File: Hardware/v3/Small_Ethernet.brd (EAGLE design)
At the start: 64.5 x 33.4 mm, 57 parts, among them U1 EDISON_CONNECTOR_FULLMOUNTING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, U2 LAN9512-JZX, U3 MAX4995AAUT+, U4 EDISON_CONNECTOR_FULLHEADER, X1 J1011F01P

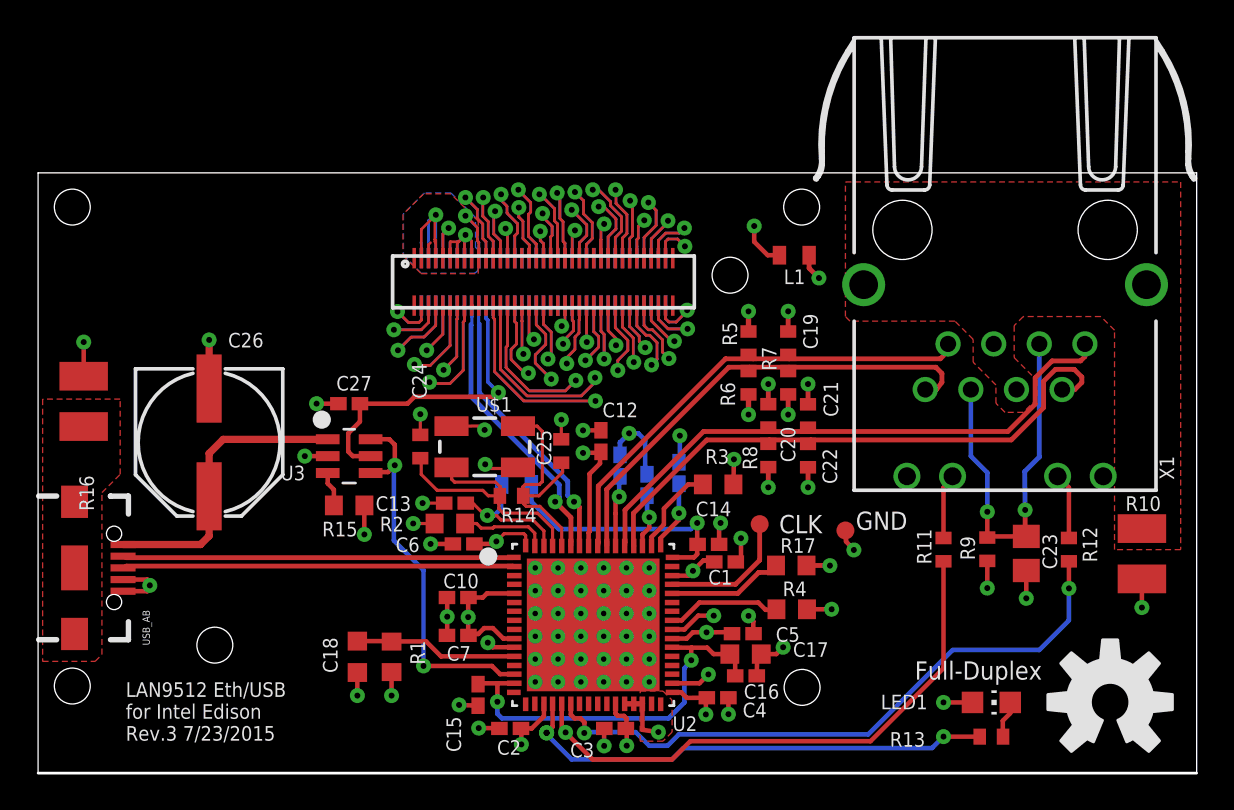
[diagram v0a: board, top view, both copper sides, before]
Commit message: Added ground fills. PoE: power planes around U7, diode for power through microB. Small: changed C26 to 2 caps, removed NP caps, removed test points, replaced crystal
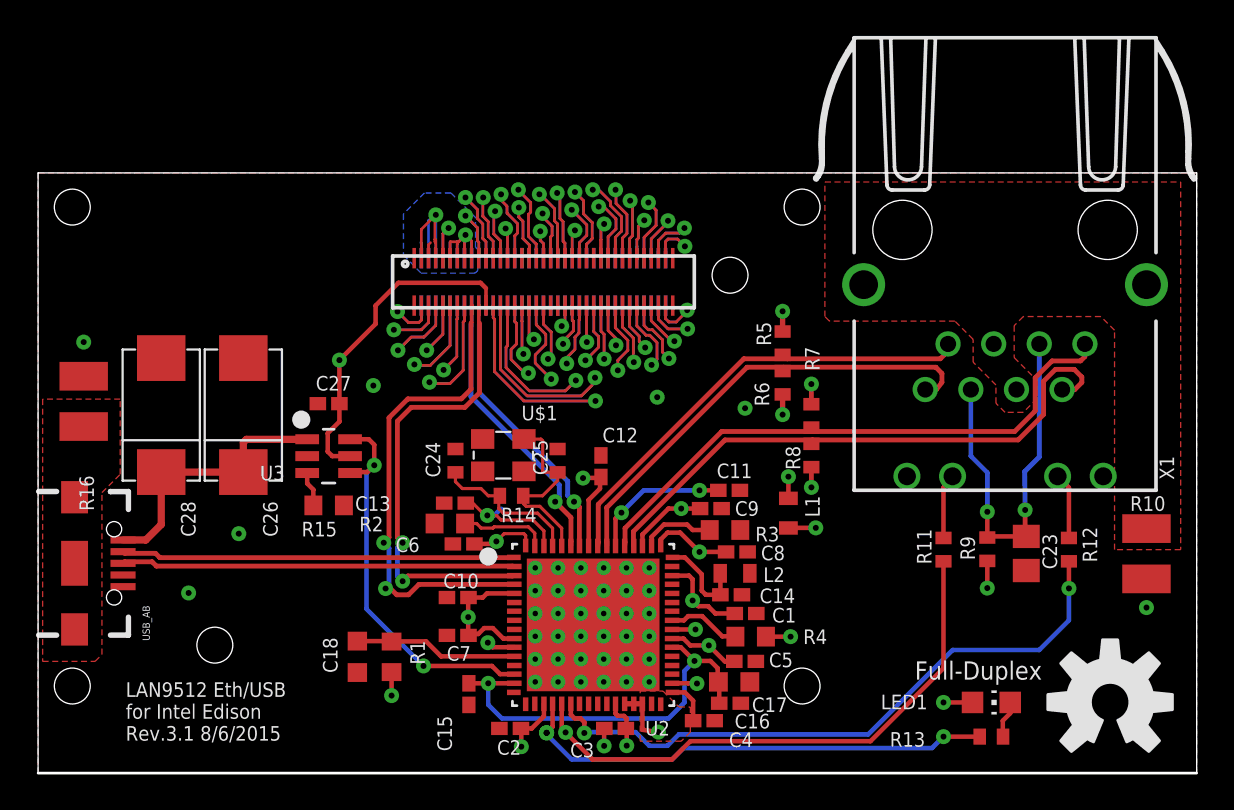
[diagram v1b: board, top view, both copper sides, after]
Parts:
- removed C19, C20, C21, C22: 15pF, rcl:C0402
- removed CLK_PAD: CLK, testpad:TP10R
- removed GNDPAD: GNDPAD, testpad:TP10R
- removed R17: 10K, resistor:R0603
- added C28: (no value), PoEdev:CAP-2917
- C26: value 150uF -> (none); device SparkFun-Capacitors:PANASONIC_E -> PoEdev:CAP-2917
- U$1: value 25MHz -> (none); device SparkFun-FreqCtrl:CRYSTAL-SMD-5X3 -> PoEdev:SMDCRYSTAL_3.2X2.5
- moved L1 14.4 mm to (41.8, 14.5), turned to 90 degrees
- moved L2 13.1 mm to (38.8, 11.1), flipped to the top
- moved C11 6.23 mm to (38.5, 15.7), flipped to the top, turned to 0 degrees
- moved C8 5.45 mm to (38.9, 12.3), flipped to the top, turned to 0 degrees
- moved C9 3.80 mm to (37.5, 14.7), flipped to the top, turned to 0 degrees
- moved C1 3.09 mm to (39.4, 8.89)
- moved C14 3.08 mm to (38.6, 9.93)
- moved R4 2.75 mm to (39.7, 7.60)
- moved R3 2.57 mm to (38.3, 13.5)
- moved C26 2.44 mm to (11.4, 19.9)
- moved R7 2.40 mm to (43.1, 19.9)
- moved R8 2.40 mm to (43.1, 17.7)
- moved C24 2.11 mm to (23.2, 17.4)
- moved R5 1.90 mm to (41.5, 23.9)
- moved R6 1.90 mm to (41.5, 21.7)
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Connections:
- removed net S$3: U4.16
- removed net S$6: U4.20
- new net USB_D_N: U2.3, U4.18
- new net USB_D_P: U2.4, U4.16
- net CLKOUT: no longer CLK_PAD.TP
- net GND: now also C26.NEG, C28.NEG, U$1.P2_GND, U$1.P4_GND; no longer C19.2, C20.2, C21.2, C22.2, C26.-, GNDPAD.TP, U$1.2, U$1.4, USB_AB.ID1
- net N$21: now also U$1.P1_I/O; no longer U$1.1
- net N$22: now also U$1.P3_O/I; no longer U$1.3
- net RX_N: no longer C22.1
- net RX_P: no longer C21.1
- net S$4: no longer R17.1
- net TX_N: no longer C19.1
- net TX_P: no longer C20.1
- net USB_VBUS: now also U4.20
- net VBUS_OUT: now also C26.POS, C28.POS; no longer C26.+
- net VDD3IO: no longer R17.2
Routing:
- net GND: track 78.6 -> 25.1 mm, vias 73 -> 47
- net USB_D_P: track 0.00 -> 27.4 mm, vias 0 -> 2
- net USB_D_N: track 0.00 -> 25.7 mm, vias 0 -> 2
- net N$2: track 14.2 -> 5.26 mm, vias 1 -> 0
- net CLKOUT: track 7.44 -> 0.00 mm
- net S$4: track 6.68 -> 0.00 mm
- net N$21: track 15.0 -> 8.48 mm
- net N$22: track 13.4 -> 10.5 mm
- net N$9: track 6.39 -> 4.10 mm
- net N$1: track 8.11 -> 6.75 mm
- net VBUS_OUT: track 16.5 -> 15.3 mm
- net USB_VBUS: track 17.4 -> 18.4 mm
- net N$8: track 5.10 -> 4.16 mm
- net TX_N: track 26.9 -> 26.1 mm
- net TX_P: track 26.9 -> 26.0 mm
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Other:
- board text added: "LAN9512 Eth/USB for Intel Edison Rev.3.1 8/6/2015"
- board text removed: "CLK"
- board text removed: "GND"
- board text removed: "LAN9512 Eth/USB for Intel Edison Rev.3 7/23/2015"

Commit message: Ready for final review
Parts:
- moved L1 3.78 mm to (43.1, 10.9)
- moved C26 2.85 mm to (12.4, 17.3)
- moved C28 2.85 mm to (7.87, 17.3)
- moved C23 1.82 mm to (55.0, 10.4)
- moved R9 1.80 mm to (52.8, 10.7)
- moved R6 1.78 mm to (41.5, 20.0)
- moved U1 1.78 mm to (40.5, 28.9)
- moved R10 1.78 mm to (61.7, 10.4)
- moved R11 1.78 mm to (50.4, 10.7)
- moved R12 1.78 mm to (57.4, 10.7)
- moved R8 1.78 mm to (43.1, 15.9)
- moved R5 1.78 mm to (41.5, 22.2)
- moved R7 1.78 mm to (43.1, 18.1)
- moved U4 1.78 mm to (28.1, 25.6)
- moved X1 1.78 mm to (53.8, 22.1)
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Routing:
- net N$1: track 6.75 -> 27.5 mm, vias 1 -> 2
- net P24: track 20.0 -> 5.62 mm
- net P26: track 16.3 -> 3.11 mm
- net P22: track 20.0 -> 9.33 mm
- net USB_D_P: track 27.4 -> 24.1 mm
- net USB_D_N: track 25.7 -> 22.4 mm
- net P12: track 7.80 -> 4.94 mm
- net VDD33A: track 52.9 -> 55.5 mm
- net P14: track 11.7 -> 9.17 mm
- net USB_VBUS: track 18.4 -> 16.3 mm
- net N$21: track 8.48 -> 10.4 mm
- net P6: track 7.56 -> 9.38 mm
- net USBUP_P: track 16.0 -> 14.2 mm
- net N$18: track 35.6 -> 33.9 mm
- net USBUP_N: track 15.7 -> 14.0 mm
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- added copper zone on layer 3, net GND
- removed copper zone on layer 3, net USB_REF
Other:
- board size 64.5 x 33.4 mm -> 64.5 x 31.6 mm

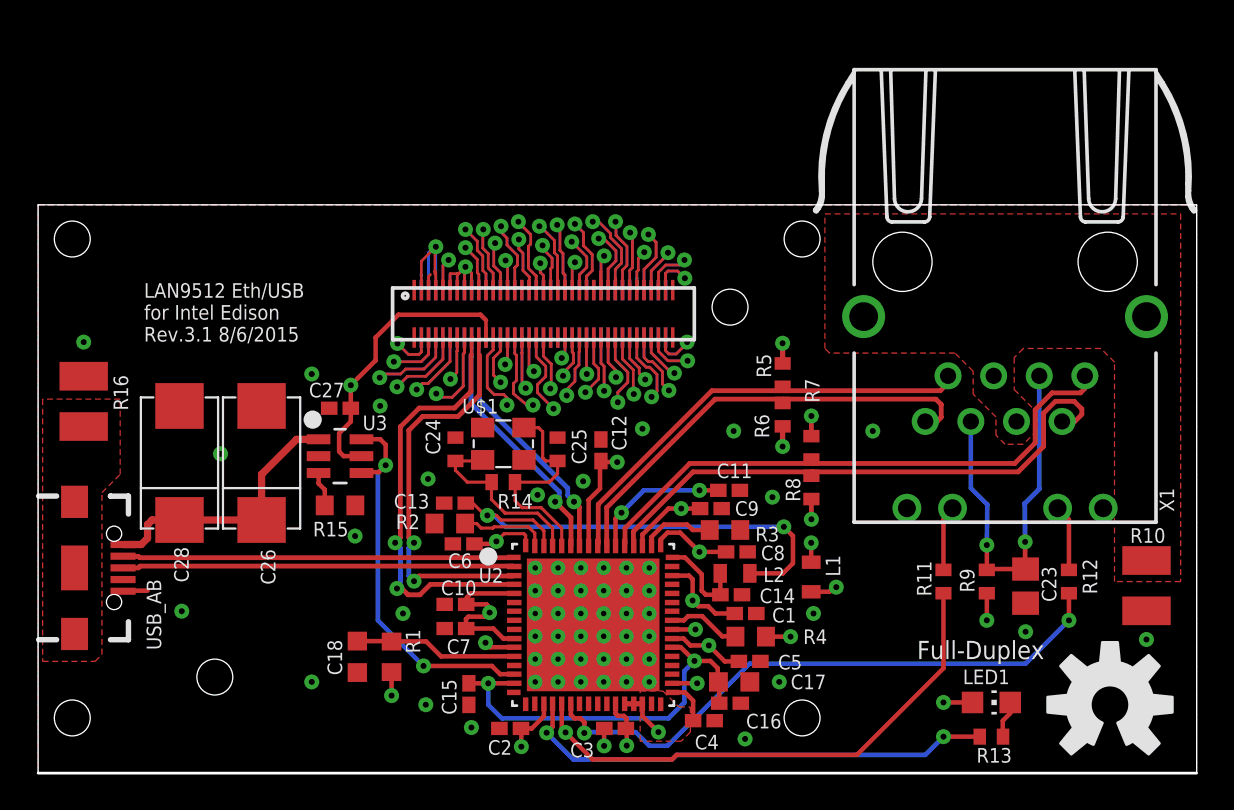
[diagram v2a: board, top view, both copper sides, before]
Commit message: Made downstream USB traces the same length; minor changes to PoE board
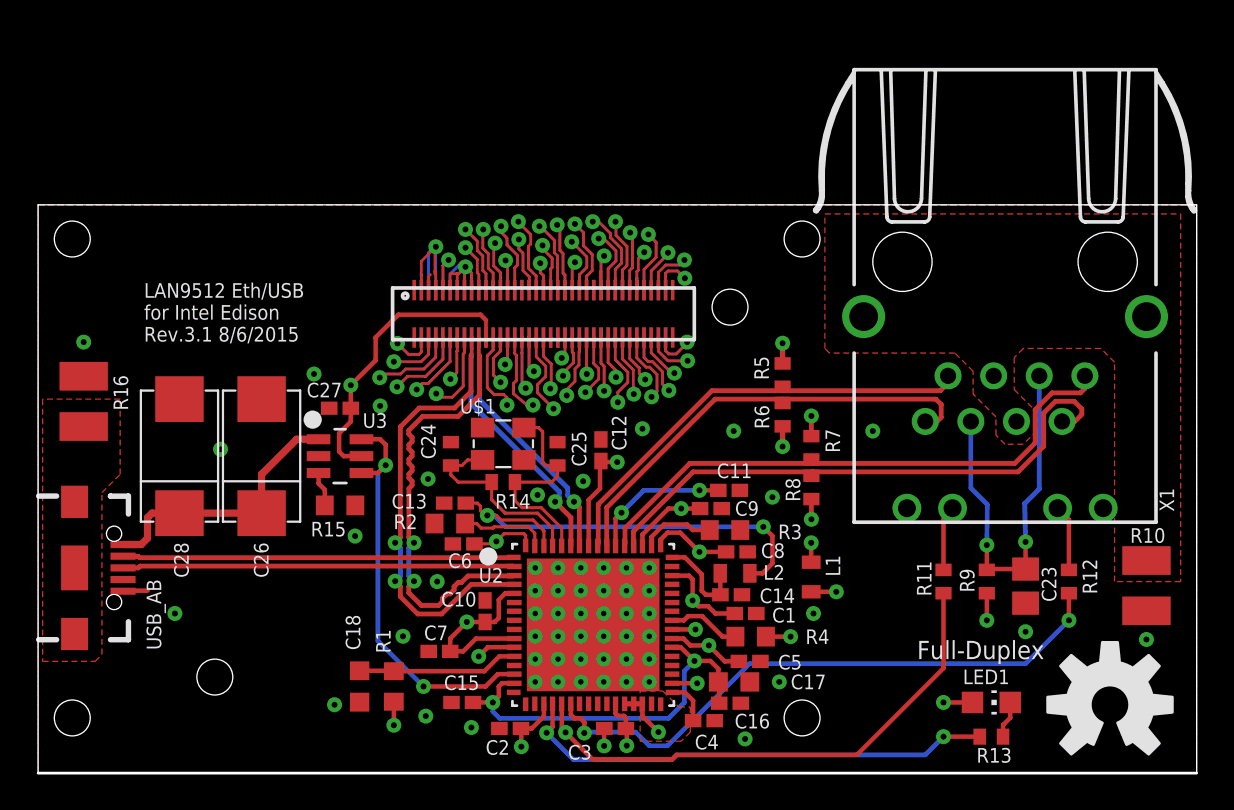
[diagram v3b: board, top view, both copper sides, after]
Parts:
- moved C10 1.69 mm to (24.9, 9.02), turned to 90 degrees
- moved R1 1.66 mm to (19.8, 4.83)
- moved C18 1.66 mm to (17.9, 4.83)
- moved C7 1.55 mm to (22.4, 6.78)
- moved C15 0.59 mm to (23.6, 3.94), turned to 180 degrees
- moved C26 0.38 mm to (12.4, 17.7)
- moved C28 0.38 mm to (7.87, 17.7)
- moved C24 0.36 mm to (23.0, 17.8)
- moved C25 0.25 mm to (28.9, 17.8)
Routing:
- net USB_D_N: track 22.4 -> 25.1 mm
- net N$1: track 27.5 -> 25.3 mm
- net N$23: track 21.8 -> 23.0 mm
- net USB_D_P: track 24.1 -> 25.2 mm
- net GND: track 26.5 -> 27.4 mm, vias 62 -> 63
- net N$4: track 22.9 -> 22.3 mm
- net N$21: track 10.4 -> 10.9 mm

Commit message: Fixed stub traces around Edison connector
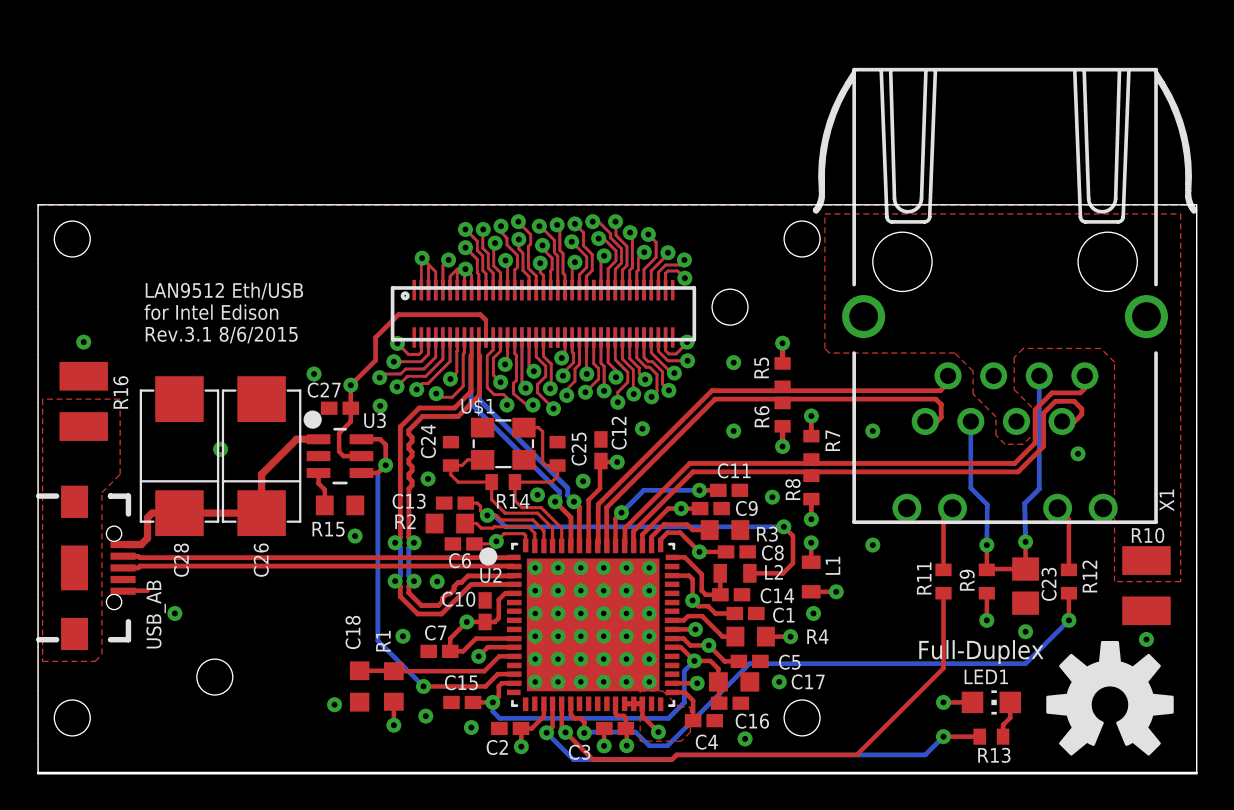
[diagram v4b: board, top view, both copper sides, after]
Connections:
- removed net P47: U1.47
- removed net S$10: U4.61
- removed net S$5: U4.70
- removed net S$7: U4.68
- removed net S$8: U1.68
- removed net S$9: U1.53
- new net GP28_I2C_6_SDA: U1.47, U4.47
- new net P68: U1.68, U4.68
- net P37: now also U1.37
- net P41: now also U1.41
- net P43: now also U1.43
- net P53: now also U1.53
- net P61: now also U4.61
- net P70: now also U4.70
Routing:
- net USB_VBUS: track 16.3 -> 27.3 mm
- net S$9: track 7.10 -> 0.00 mm, vias 1 -> 0
- net P53: track 0.51 -> 7.23 mm, vias 0 -> 1
- net P61\: track 4.30 -> 0.00 mm, vias 1 -> 0
- net P61: track 0.66 -> 4.56 mm, vias 0 -> 1
- net N$1: track 25.3 -> 27.6 mm
- net GND: track 27.4 -> 25.5 mm, vias 63 -> 66
- net P55: track 10.9 -> 9.62 mm
- net P51: track 4.87 -> 3.96 mm
- net P47: track 0.83 -> 0.00 mm
- net GP28_I2C_6_SDA: track 7.63 -> 8.43 mm
- net P7: track 4.15 -> 3.62 mm

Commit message: Added LDO for power off VSYS (to ensure enough current to LAN); Added datasheets for LDO and FTDI chip
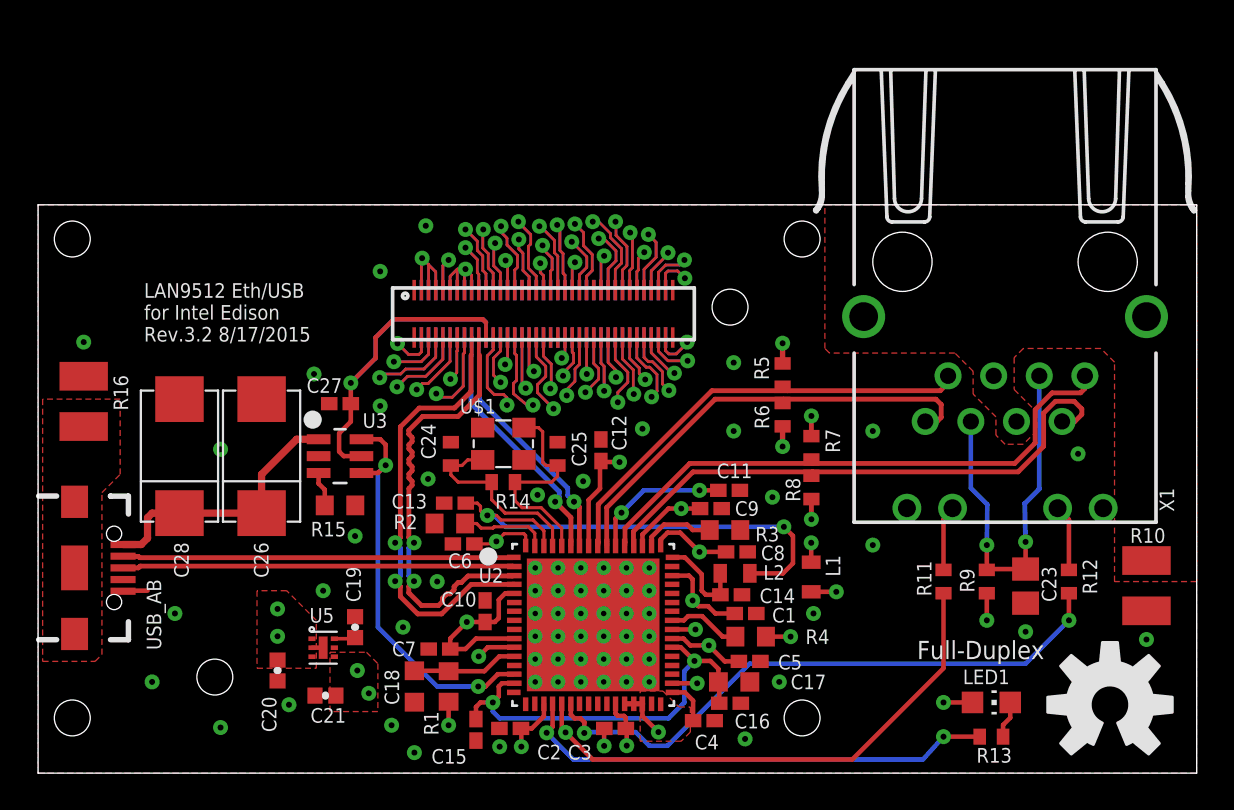
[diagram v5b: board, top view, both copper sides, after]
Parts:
- added C19: .1uF, SparkFun-Capacitors:0402-CAP
- added C20, C21: 1uF, SparkFun-Capacitors:0402-CAP
- added U5: (no value), PoEdev:6-UFDFN
- moved C18 3.05 mm to (21.0, 4.83)
- moved R1 3.05 mm to (22.9, 4.83)
- moved C15 1.70 mm to (24.4, 2.41), turned to 270 degrees
- moved C27 0.25 mm to (16.8, 20.6)
- moved C7 0.13 mm to (22.4, 6.91)
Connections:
- removed net P2: U1.2, U4.2
- removed net P4: U1.4, U4.4
- removed net P6: U1.6, U4.6
- new net BYP: C19.1, U5.P6
- new net S$5: U1.10, U1.8, U4.10, U4.8
- new net VSYS: C20.2, U1.2, U1.4, U1.6, U4.2, U4.4, U4.6, U5.P1, U5.P3
- net GND: now also C19.2, C20.1, C21.2, U5.GND, U5.P2
- net VDD3IO: now also C21.1, U5.P4; no longer U1.10, U1.8, U4.10, U4.8
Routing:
- net VSYS: track 0.00 -> 20.4 mm, vias 0 -> 5
- net S$5: track 0.00 -> 16.5 mm, vias 0 -> 2
- net VDD3IO: track 46.4 -> 29.9 mm
- net P6: track 9.38 -> 0.00 mm, vias 1 -> 0
- net P4: track 6.13 -> 0.00 mm, vias 1 -> 0
- net P2: track 4.89 -> 0.00 mm, vias 1 -> 0
- net N$7: track 8.96 -> 5.92 mm
- net BYP: track 0.00 -> 1.18 mm
- net USB_VBUS: track 27.3 -> 26.6 mm
- net GND: track 25.5 -> 26.1 mm, vias 66 -> 72
- net N$4: track 22.3 -> 22.9 mm
- added copper zone on layer 1, net VSYS
- added copper zone on layer 3, net VSYS
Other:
- board text added: "LAN9512 Eth/USB for Intel Edison Rev.3.2 8/17/2015"
- board text removed: "LAN9512 Eth/USB for Intel Edison Rev.3.1 8/6/2015"

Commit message: Aesthetic changes for Ryan
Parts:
- moved C9 1.27 mm to (38.7, 14.7)
- moved C6 0.79 mm to (22.9, 12.8)
- moved C1 0.75 mm to (38.7, 9.25)
- moved C18 0.64 mm to (21.6, 4.83)
- moved R4 0.51 mm to (39.4, 8.00)
- moved R3 0.49 mm to (38.7, 13.6)
- moved C13 0.30 mm to (22.9, 15.0)
- moved C5 0.28 mm to (39.4, 6.35)
- moved C14 0.27 mm to (38.7, 10.2)
- moved R1 0.25 mm to (23.1, 4.83)
- moved C23 0.25 mm to (55.0, 10.2)
- moved R11 0.25 mm to (50.4, 10.4)
- moved R12 0.25 mm to (57.4, 10.4)
- moved R9 0.25 mm to (52.8, 10.4)
- moved C11 0.25 mm to (38.7, 15.7)
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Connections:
- new net S$6: U1.8, U4.8
- net S$5: no longer U1.8, U4.8
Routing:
- net S$6: track 0.00 -> 8.80 mm, vias 0 -> 1
- net S$5: track 16.5 -> 7.71 mm, vias 2 -> 1
- net VDD33A: track 55.5 -> 57.5 mm
- net GND: track 26.1 -> 27.5 mm, vias 72 -> 71
- net VDD3IO: track 29.9 -> 29.1 mm
- net N$7: track 5.92 -> 5.27 mm
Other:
- board text added: "LAN9512 Eth/USB for Intel Edison Rev.3.2 8/19/2015"
- board text removed: "LAN9512 Eth/USB for Intel Edison Rev.3.2 8/17/2015"
